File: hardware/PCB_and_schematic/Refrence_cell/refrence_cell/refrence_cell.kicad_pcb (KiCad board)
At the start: 2 copper layers, 99 x 99 mm, 52 parts, among them J1 ICP_DEBUG, J2 DS18B20, J3 DS18B20, J4 DS18B20, J5 RS485, J6 Conn_01x02, J7 Conn_01x02, Q1 BC817, Q2 BC327, Q3 BC337, U1 PIC16F886-IP, U2 TL431LP, U3 ST485, U4 LM358, U5 MP1584-Step-Down

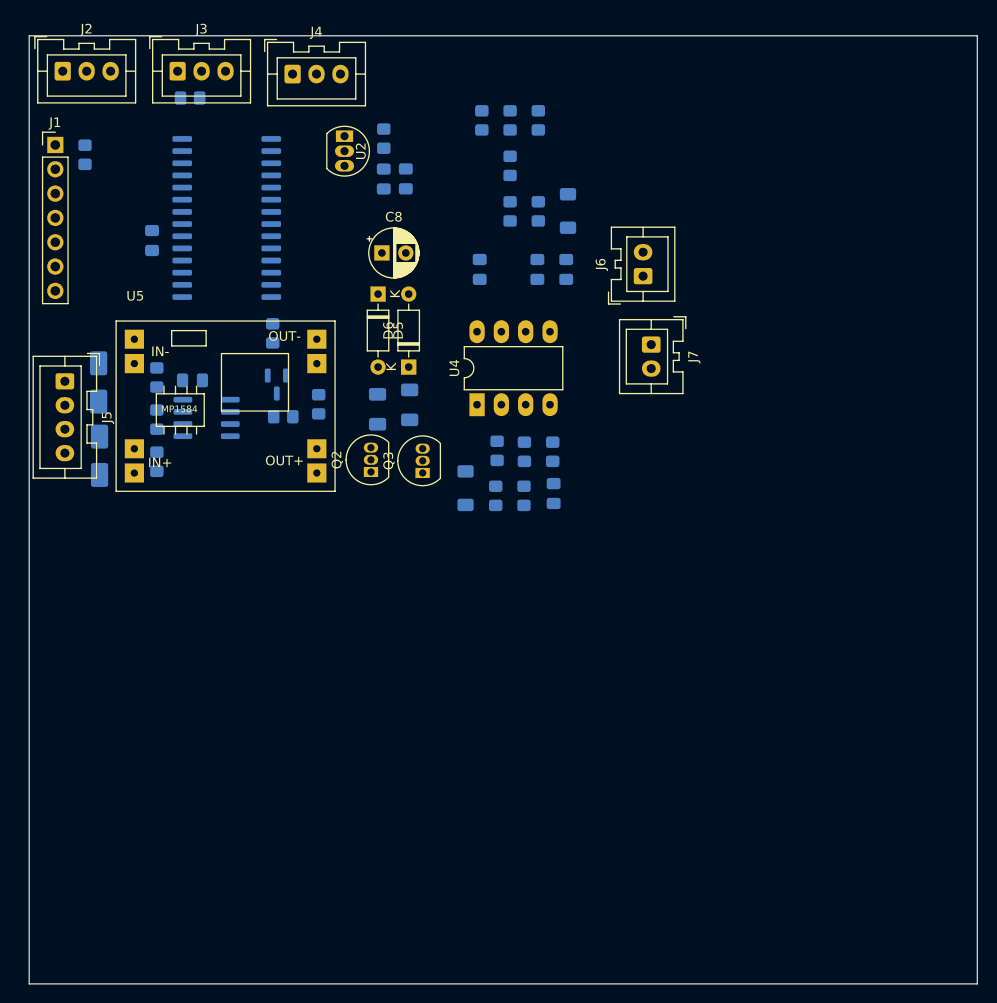
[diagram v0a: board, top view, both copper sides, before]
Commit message: add refrence cell pcb
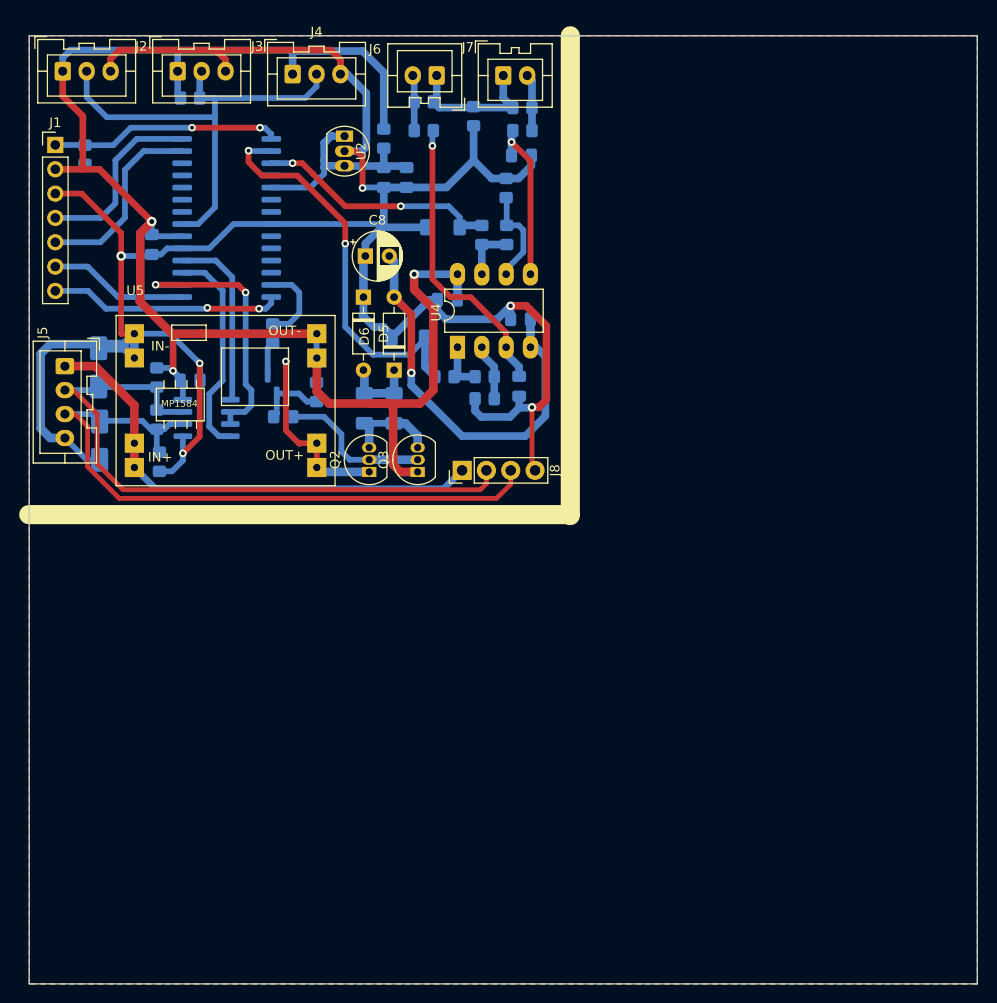
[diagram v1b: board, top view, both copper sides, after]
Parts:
- added J8: RS485, My-Footprints-connectors:PinHeader_1x04_P2.54mm_Vertical_littleBigger, F.Cu at (59.2, 96.4)
- moved R9 38.0 mm to (55.2, 57.9), turned to 0 degrees
- moved R10 36.1 mm to (55.2, 60.9), turned to 0 degrees
- moved J7 32.1 mm to (63.5, 55.1), turned to 0 degrees
- moved J6 30.1 mm to (56.5, 55.1), turned to 180 degrees
- moved D4 16.8 mm to (53.6, 82.5), turned to 180 degrees
- moved D3 13.2 mm to (57.2, 71.0), turned to 180 degrees
- moved R20 13.1 mm to (61.6, 86.6), turned to 0 degrees
- moved C10 12.8 mm to (57.7, 78.6), turned to 180 degrees
- moved C4 12.7 mm to (65.4, 63.5), turned to 0 degrees
- moved C5 11.8 mm to (65.2, 87.6)
- moved R19 10.2 mm to (61.6, 88.9), turned to 0 degrees
- moved R11 9.49 mm to (57.4, 86.6), turned to 180 degrees
- moved R12 7.79 mm to (61.3, 71.8), turned to 90 degrees
- moved U4 6.34 mm to (58.7, 83.5)
- moved C9 5.49 mm to (65.3, 80.6), turned to 180 degrees
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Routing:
- net GND: track 0.00 -> 271.4 mm, vias 0 -> 7
- net +5V: track 0.00 -> 181.7 mm, vias 0 -> 3
- net /RS485_A: track 0.00 -> 70.4 mm
- net /RS485_B: track 0.00 -> 68.9 mm
- net +24V: track 0.00 -> 51.4 mm
- net DS18B20_DATA: track 0.00 -> 51.0 mm
- net -2V5: track 0.00 -> 42.6 mm, vias 0 -> 1
- net ADC_CELL_1: track 0.00 -> 42.0 mm, vias 0 -> 2
- net Net-(U4A-+): track 0.00 -> 30.7 mm, vias 0 -> 1
- net RS232_DIR: track 0.00 -> 28.3 mm, vias 0 -> 2
- net ADC_CELL_2: track 0.00 -> 25.5 mm, vias 0 -> 2
- net I2C_DBG_SCL: track 0.00 -> 24.3 mm, vias 0 -> 2
- net RST: track 0.00 -> 24.1 mm, vias 0 -> 2
- net VREF_2V5: track 0.00 -> 23.5 mm
- net RS232_TX: track 0.00 -> 22.4 mm
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- added copper zone on B.Cu, net GND
- added copper zone on F.Cu, net GND

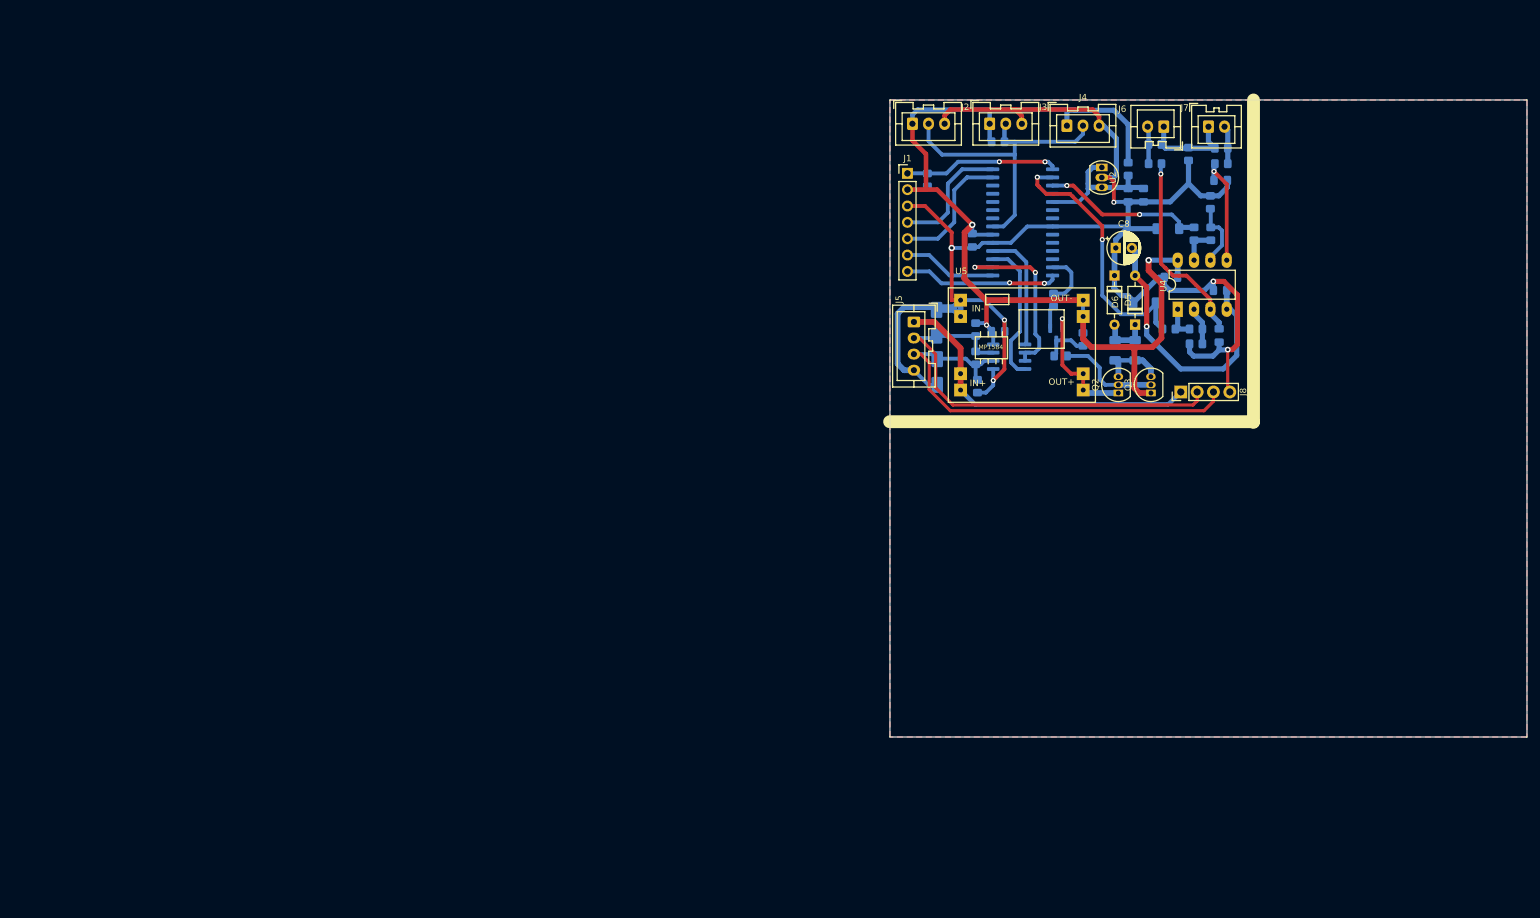
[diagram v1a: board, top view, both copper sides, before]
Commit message: add bms pcb balacer and smps separated
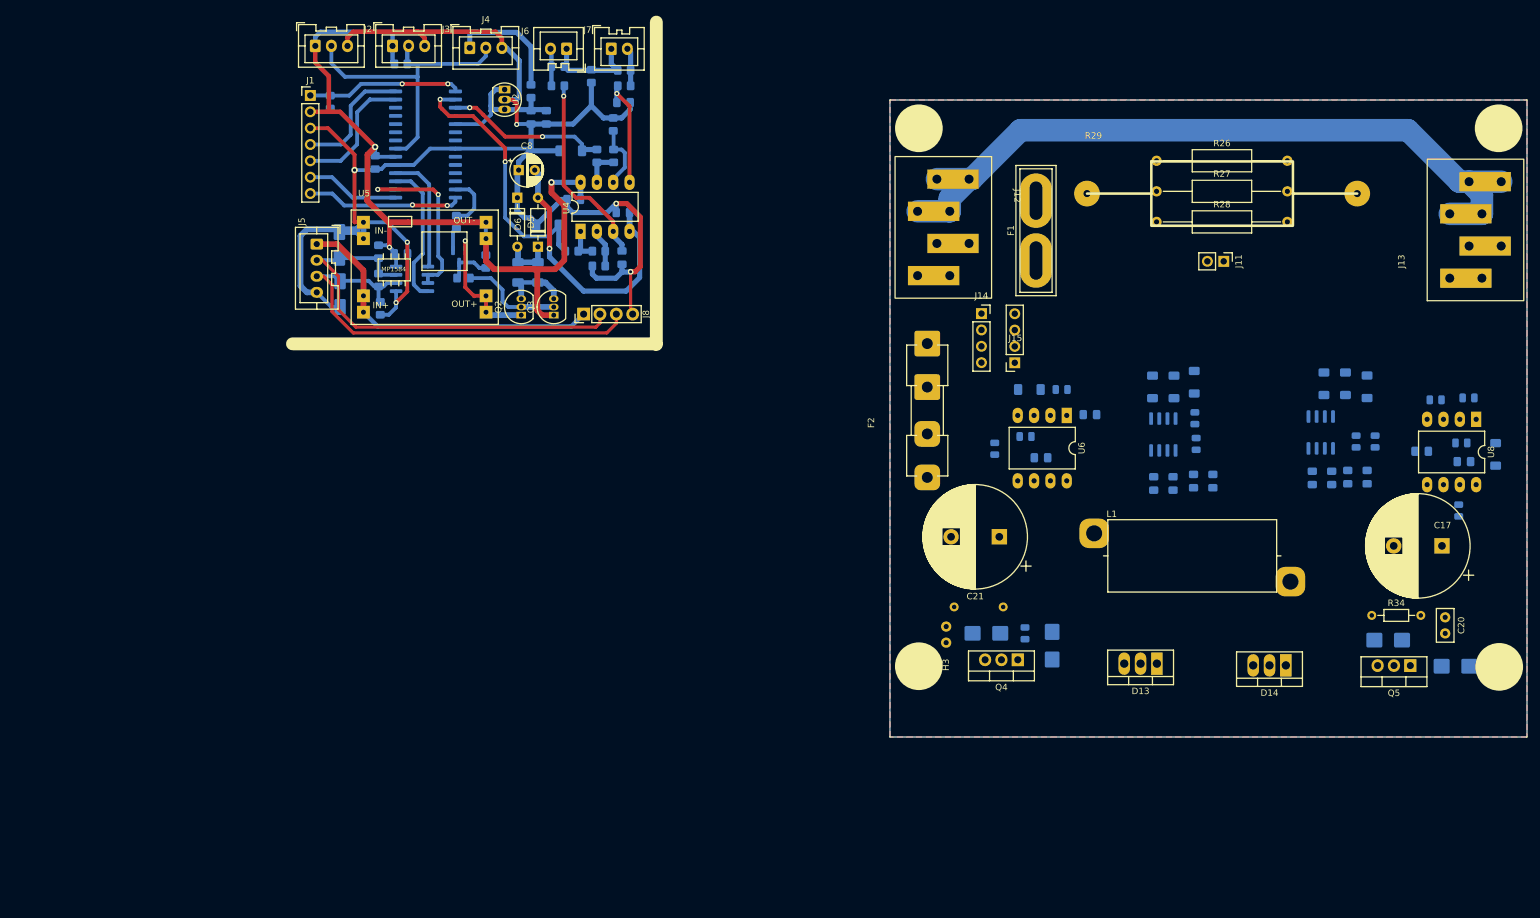
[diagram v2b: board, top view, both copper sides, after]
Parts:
- added C12: 100n, Capacitor_SMD:C_0805_2012Metric_Pad1.18x1.45mm_HandSolder, B.Cu at (45.1, 99.9)
- added C13: 10n, Capacitor_SMD:C_0805_2012Metric_Pad1.18x1.45mm_HandSolder, B.Cu at (55.0, 110.6)
- added C14: 10n, Capacitor_SMD:C_0805_2012Metric_Pad1.18x1.45mm_HandSolder, B.Cu at (58.0, 110.6)
- added C15: 100n, Capacitor_SMD:C_0805_2012Metric_Pad1.18x1.45mm_HandSolder, B.Cu at (37.5, 106.6)
- added C16: 1n, Capacitor_SMD:C_0805_2012Metric_Pad1.18x1.45mm_HandSolder, B.Cu at (61.2, 110.2)
- added C17: 100u/35V, Capacitor_THT:CP_Radial_D16.0mm_P7.50mm, F.Cu at (99.8, 120.3)
- added C18: 100n, Capacitor_SMD:C_0805_2012Metric_Pad1.18x1.45mm_HandSolder, B.Cu at (64.2, 110.2)
- added C19: 1u, Capacitor_THT:C_Disc_D5.0mm_W2.5mm_P2.50mm, B.Cu at (22.7, 132.8)
- added C20: 1u, Capacitor_THT:C_Disc_D5.0mm_W2.5mm_P2.50mm, F.Cu at (100.3, 131.4)
- added C21: 100u/35V, Capacitor_THT:CP_Radial_D16.0mm_P7.50mm, F.Cu at (31.0, 118.9)
- added C22: 100n, Capacitor_SMD:C_0805_2012Metric_Pad1.18x1.45mm_HandSolder, B.Cu at (96.6, 105.6)
- added C23: 10n, Capacitor_SMD:C_0805_2012Metric_Pad1.18x1.45mm_HandSolder, B.Cu at (79.6, 109.7)
- added C24: 10n, Capacitor_SMD:C_0805_2012Metric_Pad1.18x1.45mm_HandSolder, B.Cu at (82.7, 109.7)
- added C25: 100n, Capacitor_SMD:C_0805_2012Metric_Pad1.18x1.45mm_HandSolder, B.Cu at (103.2, 107.2)
- added C26: 1n, Capacitor_SMD:C_0805_2012Metric_Pad1.18x1.45mm_HandSolder, B.Cu at (85.2, 109.6)
- added C27: 100n, Capacitor_SMD:C_0805_2012Metric_Pad1.18x1.45mm_HandSolder, B.Cu at (88.2, 109.6)
- added D10: BZV55B15, Diode_SMD:D_MiniMELF, B.Cu at (61.3, 94.9)
- added D11: SM6T15A, Diode_SMD:D_SMB, B.Cu at (39.2, 135.8)
- added D12: SM6T15A, Diode_SMD:D_SMB, B.Cu at (29.0, 133.9)
- added D13: YM3045, My-Footprints:TO-220-3_V_Thick_Pads, F.Cu at (55.5, 138.6)
- added D14: YM3045, My-Footprints:TO-220-3_V_Thick_Pads, F.Cu at (75.5, 138.9)
- added D15: SM6T15A, Diode_SMD:D_SMB, B.Cu at (91.4, 134.9)
- added D16: SM6T15A, Diode_SMD:D_SMB, B.Cu at (101.9, 139.0)
- added D17: LL4148, Diode_SMD:D_MiniMELF, B.Cu at (81.5, 95.1)
- added D18: LL4148, Diode_SMD:D_MiniMELF, B.Cu at (84.8, 95.1)
- added D19: LL4148, Diode_SMD:D_MiniMELF, B.Cu at (108.1, 106.1)
- added D20: BZV55B15, Diode_SMD:D_MiniMELF, B.Cu at (88.2, 95.6)
- added D7: LL4148, Diode_SMD:D_MiniMELF, B.Cu at (54.8, 95.6)
- added D8: LL4148, Diode_SMD:D_MiniMELF, B.Cu at (58.1, 95.6)
- added D9: LL4148, Diode_SMD:D_MiniMELF, B.Cu at (35.7, 96.0)
- added F1: 6,3A, My-Footprints:Fuse_Blade_ATO_directSolder, F.Cu at (36.7, 76.0)
- added F2: 2A, My-Footprints:Fuseholder_Clip-5x20mm_Eaton_1A5601-01_Inline_P20.80x6.76mm_D1.70mm_Horizontal, F.Cu at (19.8, 109.7)
- added H1: MountingHole, My-Footprints:Mount-Hole-3mm, F.Cu at (18.5, 55.4)
- added H2: MountingHole, My-Footprints:Mount-Hole-3mm, F.Cu at (108.6, 55.4)
- added H3: MountingHole, My-Footprints:Mount-Hole-3mm, F.Cu at (18.5, 139.0)
- added H4: MountingHole, My-Footprints:Mount-Hole-3mm, F.Cu at (108.7, 139.1)
- added J11: R-Shunt, Connector_PinHeader_2.54mm:PinHeader_1x02_P2.54mm_Vertical, F.Cu at (65.9, 76.1)
- added J12: BATT_IN, My-Footprints-connectors:Flat-6,3mm-connector-4P, F.Cu at (29.8, 59.8)
- added J13: BATT_OUT, My-Footprints-connectors:Flat-6,3mm-connector-4P, F.Cu at (97.5, 82.2)
- added J14: batt-24V-balancer, Connector_PinSocket_2.54mm:PinSocket_1x04_P2.54mm_Vertical, F.Cu at (28.2, 84.2)
- added J15: pwm-12v-local, Connector_PinSocket_2.54mm:PinSocket_1x04_P2.54mm_Vertical, F.Cu at (33.4, 91.8)
- added L1: L, My-Footprints:Inductor_Toroidal, F.Cu at (45.7, 121.8)
- added Q4: IRF540N, Package_TO_SOT_THT:TO-220-3_Vertical, F.Cu at (33.9, 138.0)
- added Q5: IRF540N, Package_TO_SOT_THT:TO-220-3_Vertical, F.Cu at (94.9, 138.9)
- added R21: 10k, Resistor_SMD:R_0805_2012Metric, B.Cu at (30.3, 105.2)
- added R22: 10k, Resistor_SMD:R_0805_2012Metric, B.Cu at (35.1, 103.3)
- added R23: 10R, Resistor_SMD:R_0805_2012Metric, B.Cu at (40.7, 96.0)
- added R24: 100k, Resistor_SMD:R_0805_2012Metric, B.Cu at (61.6, 104.5)
- added R26: 20A/75mV, Resistor_THT:R_Axial_DIN0309_L9.0mm_D3.2mm_P20.32mm_Horizontal, F.Cu at (55.4, 60.5)
- added R27: 20A/75mV, Resistor_THT:R_Axial_DIN0309_L9.0mm_D3.2mm_P20.32mm_Horizontal, F.Cu at (55.4, 65.2)
- added R28: 20A/75mV, Resistor_THT:R_Axial_DIN0309_L9.0mm_D3.2mm_P20.32mm_Horizontal, F.Cu at (55.4, 70.0)
- added R29: 20A/75mV, My-Footprints:Resistor-Power-5W-L22-W10, F.Cu at (42.6, 65.5)
- added R31: 10R, Resistor_SMD:R_0805_2012Metric, B.Cu at (35.0, 133.9)
- added R32: 10R, Resistor_THT:R_Axial_DIN0204_L3.6mm_D1.6mm_P7.62mm_Horizontal, B.Cu at (31.6, 129.8)
- added R33: 1k, Resistor_SMD:R_0805_2012Metric, B.Cu at (61.4, 100.5)
- added R34: 10R, Resistor_THT:R_Axial_DIN0204_L3.6mm_D1.6mm_P7.62mm_Horizontal, F.Cu at (88.9, 131.1)
- added R35: 10R, Resistor_SMD:R_0805_2012Metric, B.Cu at (102.4, 114.8)
- added R36: 10k, Resistor_SMD:R_0805_2012Metric, B.Cu at (103.9, 97.3)
- added R37: 10k, Resistor_SMD:R_0805_2012Metric, B.Cu at (98.8, 97.6)
- added R38: 10R, Resistor_SMD:R_0805_2012Metric, B.Cu at (102.8, 104.3)
- added R39: 100k, Resistor_SMD:R_0805_2012Metric, B.Cu at (86.5, 104.1)
- added R41: 1k, Resistor_SMD:R_0805_2012Metric, B.Cu at (89.4, 104.1)
- added U6: FAN7382, Package_DIP:DIP-8_W10.16mm_LongPads, F.Cu at (41.5, 100.0)
- added U7: NE555D, Package_SO:SOIC-8_3.9x4.9mm_P1.27mm, B.Cu at (56.5, 103.0)
- added U8: FAN7382, Package_DIP:DIP-8_W10.16mm_LongPads, F.Cu at (105.1, 100.6)
- added U9: NE555D, Package_SO:SOIC-8_3.9x4.9mm_P1.27mm, B.Cu at (81.0, 102.7)
- moved C4 93.6 mm to (-27.4, 51.4)
- moved C6 93.6 mm to (-40.7, 77.8)
- moved C8 93.6 mm to (-43.7, 61.9)
- moved D3 93.6 mm to (-35.6, 58.9)
- moved D6 93.6 mm to (-40.7, 73.8)
- moved J1 93.6 mm to (-76.1, 50.3)
- moved J5 93.6 mm to (-75.1, 73.4)
- moved J8 93.6 mm to (-33.6, 84.3)
- moved Q1 93.6 mm to (-53.0, 75.3)
- moved Q3 93.6 mm to (-38.2, 84.4)
- moved R10 93.6 mm to (-37.6, 48.8)
- moved R5 93.6 mm to (-65.2, 83.4)
- moved R9 93.6 mm to (-37.6, 45.8)
- moved C1 93.6 mm to (-66.0, 60.7)
- moved C10 93.6 mm to (-35.1, 66.5)
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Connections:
- net /RS485_A renamed /Reference Cell/RS485_A
- net /RS485_B renamed /Reference Cell/RS485_B
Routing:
- net GNDA: track 15.2 -> 131.4 mm
